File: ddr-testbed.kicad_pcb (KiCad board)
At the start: 4 copper layers, 69.6 x 30 mm, 2 parts, among them J1 ddr4-sodimm-edge-connector, U1 MT53E256M16D1

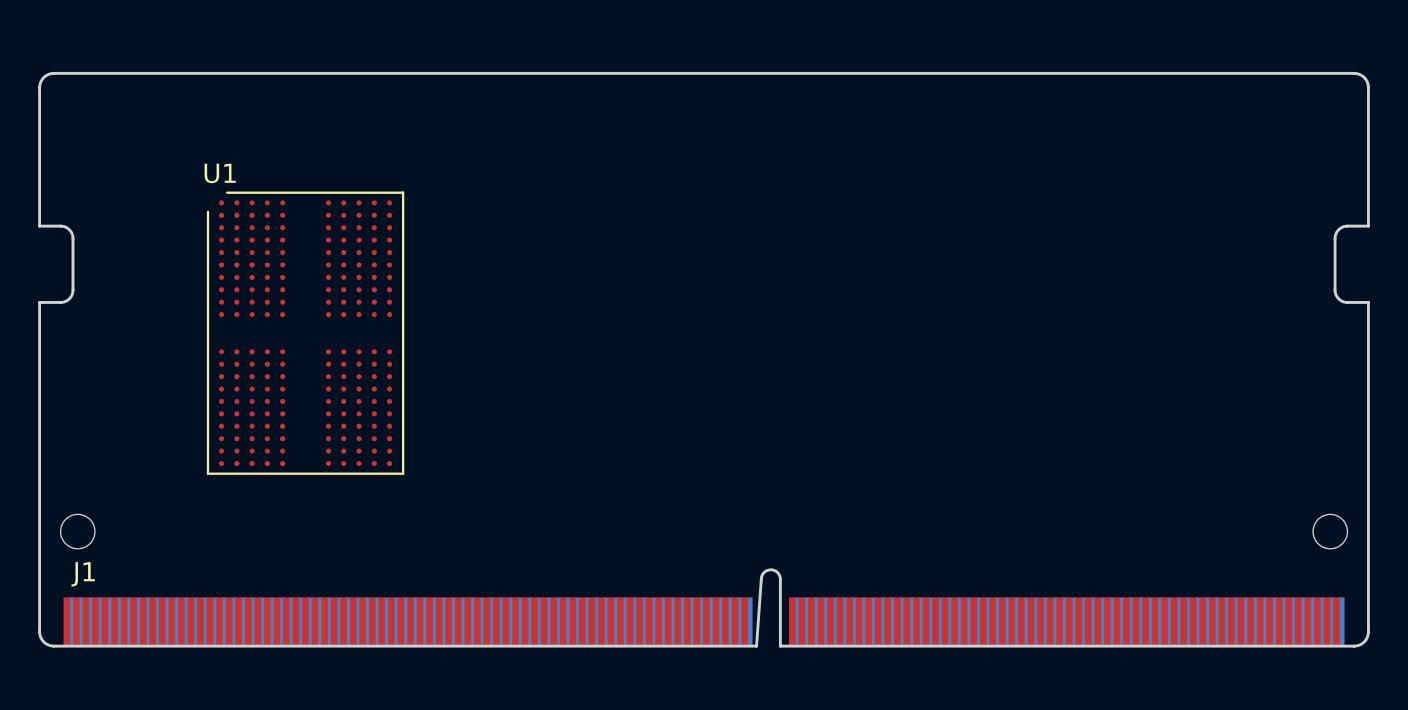
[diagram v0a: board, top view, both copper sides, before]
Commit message: Add initial component placement
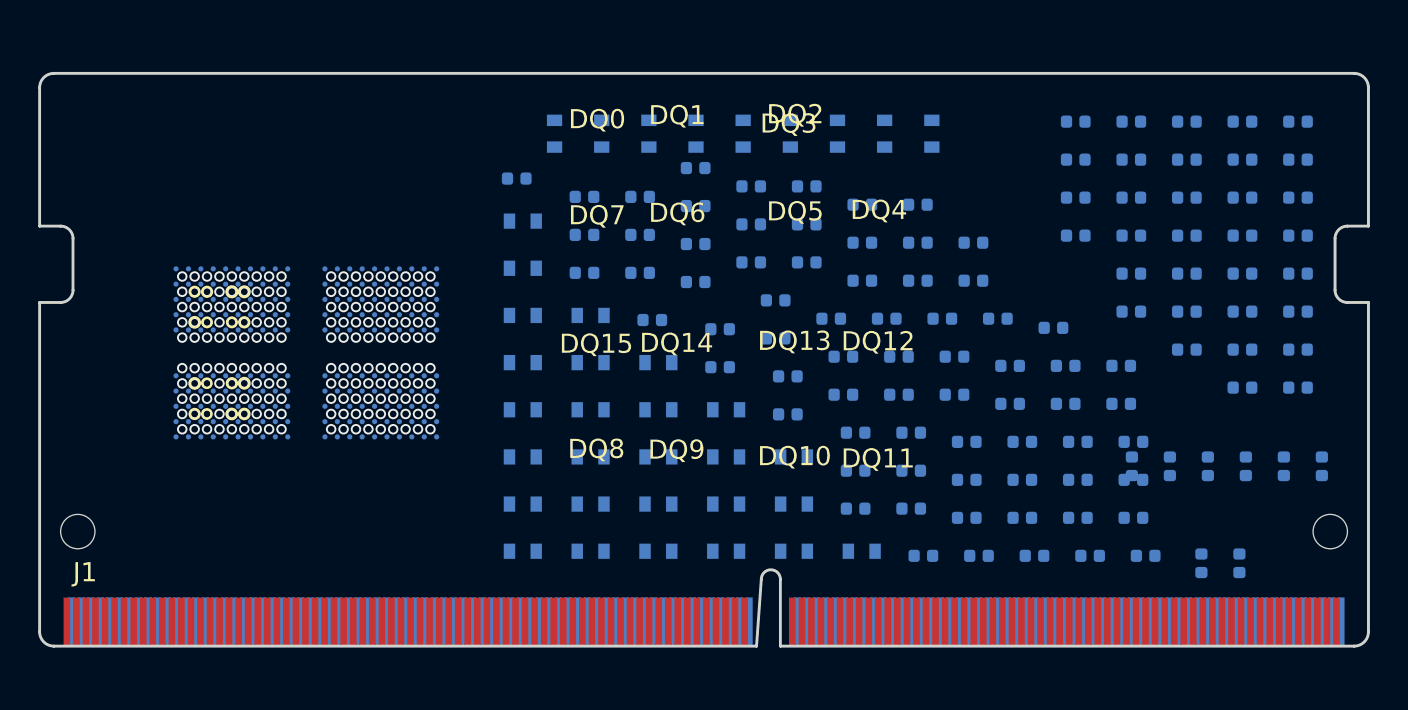
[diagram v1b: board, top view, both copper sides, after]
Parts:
- added C1: C_100p_0402, antmicro-footprints:0402-cap, B.Cu at (160.1, 76.5)
- added C10: C_10u_0603, antmicro-footprints:0603-cap, B.Cu at (136.8, 73.2)
- added C100: C_1u_0402, antmicro-footprints:0402-cap, B.Cu at (134.4, 75.0)
- added C101: C_1u_0402, antmicro-footprints:0402-cap, B.Cu at (141.5, 82.8)
- added C102: C_10u_0603, antmicro-footprints:0603-cap, B.Cu at (127.0, 73.2)
- added C103: C_10u_0603, antmicro-footprints:0603-cap, B.Cu at (139.5, 90.1)
- added C104: C_1u_0402, antmicro-footprints:0402-cap, B.Cu at (148.6, 89.3)
- added C105: C_1u_0402, antmicro-footprints:0402-cap, B.Cu at (151.5, 91.3)
- added C106: C_1u_0402, antmicro-footprints:0402-cap, B.Cu at (145.0, 84.8)
- added C107: C_1u_0402, antmicro-footprints:0402-cap, B.Cu at (134.4, 77.0)
- added C108: C_1u_0402, antmicro-footprints:0402-cap, B.Cu at (154.4, 93.3)
- added C109: C_1u_0402, antmicro-footprints:0402-cap, B.Cu at (142.7, 90.8)
- added C11: C_1u_0402, antmicro-footprints:0402-cap, B.Cu at (148.9, 78.9)
- added C110: C_1u_0402, antmicro-footprints:0402-cap, B.Cu at (147.9, 84.8)
- added C111: C_1u_0402, antmicro-footprints:0402-cap, B.Cu at (154.4, 91.3)
- added C112: C_1u_0402, antmicro-footprints:0402-cap, B.Cu at (151.5, 89.3)
- added C12: C_1u_0402, antmicro-footprints:0402-cap, B.Cu at (153.1, 83.3)
- added C13: C_10u_0603, antmicro-footprints:0603-cap, B.Cu at (132.4, 92.6)
- added C14: C_10u_0603, antmicro-footprints:0603-cap, B.Cu at (134.4, 73.2)
- added C15: C_100n_0402_6V3, antmicro-footprints:0402-cap, B.Cu at (156.7, 87.3)
- added C16: C_100n_0402_6V3, antmicro-footprints:0402-cap, B.Cu at (146.0, 76.9)
- added C17: C_1u_0402, antmicro-footprints:0402-cap, B.Cu at (145.0, 86.8)
- added C18: C_1u_0402, antmicro-footprints:0402-cap, B.Cu at (157.3, 89.3)
- added C19: C_10u_0603, antmicro-footprints:0603-cap, B.Cu at (131.9, 73.2)
- added C2: C_3p3_0402, antmicro-footprints:0402-res, B.Cu at (160.1, 72.5)
- added C20: C_10u_0603, antmicro-footprints:0603-cap, B.Cu at (136.0, 92.6)
- added C21: C_100n_0402_6V3, antmicro-footprints:0402-cap, B.Cu at (153.7, 85.3)
- added C22: C_1u_0402, antmicro-footprints:0402-cap, B.Cu at (146.0, 78.9)
- added C23: C_10u_0603, antmicro-footprints:0603-cap, B.Cu at (128.9, 87.6)
- added C24: C_100n_0402_6V3, antmicro-footprints:0402-cap, B.Cu at (157.3, 93.3)
- added C25: C_1u_0402, antmicro-footprints:0402-cap, B.Cu at (153.7, 87.3)
- added C26: C_10u_0603, antmicro-footprints:0603-cap, B.Cu at (132.4, 95.0)
- added C27: C_100n_0402_6V3, antmicro-footprints:0402-cap, B.Cu at (143.1, 76.9)
- added C28: C_1u_0402, antmicro-footprints:0402-cap, B.Cu at (157.3, 91.3)
- added C29: C_10u_0603, antmicro-footprints:0603-cap, B.Cu at (128.9, 95.0)
- added C3: C_10n_0402, antmicro-footprints:0402-cap, B.Cu at (165.2, 90.6)
- added C30: C_1u_0402, antmicro-footprints:0402-cap, B.Cu at (148.9, 80.9)
- added C31: C_100n_0402_6V3, antmicro-footprints:0402-cap, B.Cu at (143.1, 80.9)
- added C32: C_10u_0603, antmicro-footprints:0603-cap, B.Cu at (125.3, 82.7)
- added C33: C_10u_0603, antmicro-footprints:0603-cap, B.Cu at (128.9, 82.7)
- added C34: C_1u_0402, antmicro-footprints:0402-cap, B.Cu at (144.4, 82.8)
- added C35: C_100n_0402_6V3, antmicro-footprints:0402-cap, B.Cu at (137.3, 79.9)
- added C36: C_1u_0402, antmicro-footprints:0402-cap, B.Cu at (157.9, 95.3)
- added C37: C_100n_0402_6V3, antmicro-footprints:0402-cap, B.Cu at (140.2, 77.9)
- added C38: C_10u_0603, antmicro-footprints:0603-cap, B.Cu at (132.4, 87.6)
- added C39: C_10u_0603, antmicro-footprints:0603-cap, B.Cu at (128.9, 85.2)
- added C4: C_100n_0402_6V3, antmicro-footprints:0402-cap, B.Cu at (161.2, 90.6)
- added C40: C_1u_0402, antmicro-footprints:0402-cap, B.Cu at (137.3, 75.9)
- added C41: C_1u_0402, antmicro-footprints:0402-cap, B.Cu at (148.6, 91.3)
- added C42: C_100n_0402_6V3, antmicro-footprints:0402-cap, B.Cu at (142.1, 84.8)
- added C43: C_100n_0402_6V3, antmicro-footprints:0402-cap, B.Cu at (138.6, 83.9)
- added C44: C_10u_0603, antmicro-footprints:0603-cap, B.Cu at (132.4, 90.1)
- added C45: C_10u_0603, antmicro-footprints:0603-cap, B.Cu at (136.0, 95.0)
- added C46: C_1u_0402, antmicro-footprints:0402-cap, B.Cu at (125.0, 75.5)
- added C47: C_1u_0402, antmicro-footprints:0402-cap, B.Cu at (128.5, 80.5)
- added C48: C_100n_0402_6V3, antmicro-footprints:0402-cap, B.Cu at (132.1, 82.9)
- added C49: C_10u_0603, antmicro-footprints:0603-cap, B.Cu at (125.3, 95.0)
- added C5: C_1u_0402, antmicro-footprints:0402-cap, B.Cu at (151.5, 93.3)
- added C50: C_100n_0402_6V3, antmicro-footprints:0402-cap, B.Cu at (146.3, 95.3)
- added C51: C_10u_0603, antmicro-footprints:0603-cap, B.Cu at (132.4, 85.2)
- added C52: C_1u_0402, antmicro-footprints:0402-cap, B.Cu at (142.7, 92.8)
- added C53: C_10u_0603, antmicro-footprints:0603-cap, B.Cu at (139.5, 92.6)
- added C54: C_1u_0402, antmicro-footprints:0402-cap, B.Cu at (154.4, 89.3)
- added C55: C_100n_0402_6V3, antmicro-footprints:0402-cap, B.Cu at (131.4, 80.5)
- added C56: C_100n_0402_6V3, antmicro-footprints:0402-cap, B.Cu at (128.5, 78.5)
- added C57: C_10u_0603, antmicro-footprints:0603-cap, B.Cu at (139.5, 95.0)
- added C58: C_1u_0402, antmicro-footprints:0402-cap, B.Cu at (150.2, 82.8)
- added C59: C_1u_0402, antmicro-footprints:0402-cap, B.Cu at (150.8, 87.3)
- added C6: C_10u_0603, antmicro-footprints:0603-cap, B.Cu at (125.3, 90.1)
- added C60: C_10u_0603, antmicro-footprints:0603-cap, B.Cu at (136.0, 90.1)
- added C61: C_100n_0402_6V3, antmicro-footprints:0402-cap, B.Cu at (147.3, 82.8)
- added C62: C_1u_0402, antmicro-footprints:0402-cap, B.Cu at (143.1, 78.9)
- added C63: C_1u_0402, antmicro-footprints:0402-cap, B.Cu at (140.2, 75.9)
- added C64: C_10u_0603, antmicro-footprints:0603-cap, B.Cu at (125.3, 77.7)
- added C65: C_1u_0402, antmicro-footprints:0402-cap, B.Cu at (150.8, 85.3)
- added C66: C_1u_0402, antmicro-footprints:0402-cap, B.Cu at (146.0, 80.9)
- added C67: C_10u_0603, antmicro-footprints:0603-cap, B.Cu at (125.3, 87.6)
- added C68: C_1u_0402, antmicro-footprints:0402-cap, B.Cu at (134.4, 80.9)
- added C69: C_10u_0603, antmicro-footprints:0603-cap, B.Cu at (125.3, 85.2)
- added C7: C_1u_0402, antmicro-footprints:0402-cap, B.Cu at (140.2, 79.9)
- added C70: C_1u_0402, antmicro-footprints:0402-cap, B.Cu at (139.2, 85.9)
- added C71: C_1u_0402, antmicro-footprints:0402-cap, B.Cu at (142.7, 88.8)
- added C72: C_10u_0603, antmicro-footprints:0603-cap, B.Cu at (143.1, 95.0)
- added C73: C_1u_0402, antmicro-footprints:0402-cap, B.Cu at (149.2, 95.3)
- added C74: C_10u_0603, antmicro-footprints:0603-cap, B.Cu at (125.3, 80.2)
- added C75: C_1u_0402, antmicro-footprints:0402-cap, B.Cu at (135.6, 83.4)
- added C76: C_1u_0402, antmicro-footprints:0402-cap, B.Cu at (131.4, 78.5)
- added C77: C_10u_0603, antmicro-footprints:0603-cap, B.Cu at (129.4, 73.2)
- added C78: C_1u_0402, antmicro-footprints:0402-cap, B.Cu at (152.1, 95.3)
- added C79: C_1u_0402, antmicro-footprints:0402-cap, B.Cu at (128.5, 76.5)
- added C8: C_10u_0603, antmicro-footprints:0603-cap, B.Cu at (128.9, 92.6)
- added C80: C_10u_0603, antmicro-footprints:0603-cap, B.Cu at (136.0, 87.6)
- added C81: C_1u_0402, antmicro-footprints:0402-cap, B.Cu at (145.7, 92.8)
- added C82: C_1u_0402, antmicro-footprints:0402-cap, B.Cu at (145.7, 90.8)
- added C83: C_10u_0603, antmicro-footprints:0603-cap, B.Cu at (144.3, 73.2)
- added C84: C_1u_0402, antmicro-footprints:0402-cap, B.Cu at (139.2, 87.9)
- added C85: C_1u_0402, antmicro-footprints:0402-cap, B.Cu at (131.4, 76.5)
- added C86: C_10u_0603, antmicro-footprints:0603-cap, B.Cu at (125.3, 92.6)
- added C87: C_1u_0402, antmicro-footprints:0402-cap, B.Cu at (148.6, 93.3)
- added C88: C_1u_0402, antmicro-footprints:0402-cap, B.Cu at (134.4, 78.9)
- added C89: C_10u_0603, antmicro-footprints:0603-cap, B.Cu at (139.3, 73.2)
- added C9: C_100n_0402_6V3, antmicro-footprints:0402-cap, B.Cu at (156.7, 85.3)
- added C90: C_1u_0402, antmicro-footprints:0402-cap, B.Cu at (142.1, 86.8)
- added C91: C_1u_0402, antmicro-footprints:0402-cap, B.Cu at (135.6, 85.4)
- added C92: C_10u_0603, antmicro-footprints:0603-cap, B.Cu at (146.7, 73.2)
- added C93: C_1u_0402, antmicro-footprints:0402-cap, B.Cu at (138.6, 81.9)
- added C94: C_1u_0402, antmicro-footprints:0402-cap, B.Cu at (145.7, 88.8)
- added C95: C_10u_0603, antmicro-footprints:0603-cap, B.Cu at (128.9, 90.1)
- added C96: C_1u_0402, antmicro-footprints:0402-cap, B.Cu at (147.9, 86.8)
- added C97: C_1u_0402, antmicro-footprints:0402-cap, B.Cu at (155.0, 95.3)
- added C98: C_10u_0603, antmicro-footprints:0603-cap, B.Cu at (141.8, 73.2)
- added C99: C_1u_0402, antmicro-footprints:0402-cap, B.Cu at (137.3, 77.9)
- added R1: R_240R_0402, antmicro-footprints:0402-res, B.Cu at (157.2, 82.5)
- added R10: R_75R_0402, antmicro-footprints:0402-res, B.Cu at (157.2, 74.5)
- added R11: R_0R_0402, antmicro-footprints:0402-res, B.Cu at (165.9, 86.5)
- added R12: R_0R_0402, antmicro-footprints:0402-res, B.Cu at (163.0, 82.5)
- added R13: R_40R2_0402, antmicro-footprints:0402-res, B.Cu at (154.3, 74.5)
- added R14: R_40R2_0402, antmicro-footprints:0402-res, B.Cu at (165.9, 84.5)
- added R15: R_40R2_0402, antmicro-footprints:0402-res, B.Cu at (157.2, 76.5)
- added R16: R_40R2_0402, antmicro-footprints:0402-res, B.Cu at (160.1, 78.5)
- added R17: R_40R2_0402, antmicro-footprints:0402-res, B.Cu at (163.0, 80.5)
- added R18: R_40R2_0402, antmicro-footprints:0402-res, B.Cu at (167.2, 90.6)
- added R19: R_40R2_0402, antmicro-footprints:0402-res, B.Cu at (154.3, 72.5)
- added R2: R_120R_0402, antmicro-footprints:0402-res, B.Cu at (160.1, 84.5)
- added R20: R_40R2_0402, antmicro-footprints:0402-res, B.Cu at (165.9, 82.5)
- added R21: R_40R2_0402, antmicro-footprints:0402-res, B.Cu at (163.0, 78.5)
- added R22: R_40R2_0402, antmicro-footprints:0402-res, B.Cu at (165.9, 80.5)
- added R23: R_40R2_0402, antmicro-footprints:0402-res, B.Cu at (157.2, 72.5)
- added R24: R_40R2_0402, antmicro-footprints:0402-res, B.Cu at (163.2, 90.6)
- added R25: R_40R2_0402, antmicro-footprints:0402-res, B.Cu at (160.1, 74.5)
- added R26: R_40R2_0402, antmicro-footprints:0402-res, B.Cu at (163.0, 76.5)
- added R27: R_0R_0402, antmicro-footprints:0402-res, B.Cu at (165.9, 78.5)
- added R28: R_0R_0402, antmicro-footprints:0402-res, B.Cu at (160.8, 95.7)
- added R29: R_0R_0402, antmicro-footprints:0402-res, B.Cu at (160.1, 80.5)
- added R3: R_0R_0402, antmicro-footprints:0402-res, B.Cu at (154.3, 78.5)
- added R30: R_40R2_0402, antmicro-footprints:0402-res, B.Cu at (163.0, 74.5)
- added R31: R_0R_0402, antmicro-footprints:0402-res, B.Cu at (165.9, 76.5)
- added R32: R_40R2_0402, antmicro-footprints:0402-res, B.Cu at (159.2, 90.6)
- added R33: R_80R6_0402, antmicro-footprints:0402-res, B.Cu at (163.0, 72.5)
- added R34: R_80R6_0402, antmicro-footprints:0402-res, B.Cu at (165.9, 74.5)
- added R35: R_4k7_0402, antmicro-footprints:0402-res, B.Cu at (157.2, 90.6)
- added R36: R_0R_0402, antmicro-footprints:0402-res, B.Cu at (162.8, 95.7)
- added R37: R_40R2_0402, antmicro-footprints:0402-res, B.Cu at (165.9, 72.5)
- added R4: R_0R_0402, antmicro-footprints:0402-res, B.Cu at (157.2, 80.5)
- added R5: R_0R_0402, antmicro-footprints:0402-res, B.Cu at (163.0, 86.5)
- added R6: R_40R2_0402, antmicro-footprints:0402-res, B.Cu at (160.1, 82.5)
- added R7: R_40R2_0402, antmicro-footprints:0402-res, B.Cu at (163.0, 84.5)
- added R8: R_40R2_0402, antmicro-footprints:0402-res, B.Cu at (154.3, 76.5)
- added R9: R_40R2_0402, antmicro-footprints:0402-res, B.Cu at (157.2, 78.5)
- U1: moved to B.Cu
- moved U1 1.03 mm to (114.0, 84.6), turned to 270 degrees
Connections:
- net /DQ2 renamed /DQ02
- net Net-(J1-Pad113) renamed /BG0
- net Net-(J1-Pad114) renamed /ACT_N
- net Net-(J1-Pad115) renamed /BG1
- net Net-(J1-Pad134) renamed /EVENT_N
- net Net-(J1-Pad143) renamed /PARITY
- net Net-(J1-Pad145) renamed /BA1
- net Net-(J1-Pad149) renamed /CS0_N
- net Net-(J1-Pad150) renamed /BA0
- net Net-(J1-Pad253) renamed /SCL
- net Net-(J1-Pad254) renamed /SDA
- net Net-(J1-Pad255) renamed VDDSPD
- net Net-(J1-Pad256) renamed /SA0
- J1 pad 1: Net-(J1-Pad1) -> GND
- J1 pad 10: Net-(J1-Pad10) -> GND
- J1 pad 102: Net-(J1-Pad102) -> GND
- J1 pad 103: Net-(J1-Pad103) -> GND
- J1 pad 106: Net-(J1-Pad106) -> GND
- J1 pad 107: Net-(J1-Pad107) -> GND
- J1 pad 108: Net-(J1-Pad108) -> /RESET_CONN_N
- J1 pad 109: Net-(J1-Pad109) -> /CKE_0
- J1 pad 11: Net-(J1-Pad11) -> /DQS0_C
- J1 pad 110: Net-(J1-Pad110) -> /CKE_1
- J1 pad 111: Net-(J1-Pad111) -> DDRVCC
- J1 pad 112: Net-(J1-Pad112) -> DDRVCC
- J1 pad 116: Net-(J1-Pad116) -> /ALERT_N
- J1 pad 117: Net-(J1-Pad117) -> DDRVCC
- J1 pad 118: Net-(J1-Pad118) -> DDRVCC
- J1 pad 119: Net-(J1-Pad119) -> /CA2_B
- J1 pad 12: Net-(J1-Pad12) -> /DM0_N
- J1 pad 120: Net-(J1-Pad120) -> /CA1_B
- J1 pad 123: Net-(J1-Pad123) -> DDRVCC
- J1 pad 124: Net-(J1-Pad124) -> DDRVCC
- J1 pad 126: Net-(J1-Pad126) -> /CA5_A
- J1 pad 128: Net-(J1-Pad128) -> /CA4_A
- J1 pad 129: Net-(J1-Pad129) -> DDRVCC
- J1 pad 13: Net-(J1-Pad13) -> /DQS0_T
- J1 pad 130: Net-(J1-Pad130) -> DDRVCC
- J1 pad 131: Net-(J1-Pad131) -> /CA3_A
- J1 pad 132: Net-(J1-Pad132) -> /CA2_A
- J1 pad 133: Net-(J1-Pad133) -> /CA1_A
- J1 pad 135: Net-(J1-Pad135) -> DDRVCC
- J1 pad 136: Net-(J1-Pad136) -> DDRVCC
- J1 pad 137: Net-(J1-Pad137) -> /CK0_T
- J1 pad 138: Net-(J1-Pad138) -> /CK1_T
- J1 pad 139: Net-(J1-Pad139) -> /CK0_C
- J1 pad 14: Net-(J1-Pad14) -> GND
- J1 pad 140: Net-(J1-Pad140) -> /CK1_C
- J1 pad 141: Net-(J1-Pad141) -> DDRVCC
- J1 pad 142: Net-(J1-Pad142) -> DDRVCC
- J1 pad 144: Net-(J1-Pad144) -> /CA0_A
- J1 pad 146: Net-(J1-Pad146) -> /CA0_B
- J1 pad 147: Net-(J1-Pad147) -> DDRVCC
- J1 pad 148: Net-(J1-Pad148) -> DDRVCC
- J1 pad 15: Net-(J1-Pad15) -> GND
- J1 pad 151: Net-(J1-Pad151) -> /CA4_B
- J1 pad 153: Net-(J1-Pad153) -> DDRVCC
- J1 pad 154: Net-(J1-Pad154) -> DDRVCC
- J1 pad 155: Net-(J1-Pad155) -> /ODT0
- J1 pad 156: Net-(J1-Pad156) -> /CA5_B
- J1 pad 157: Net-(J1-Pad157) -> /CS_1_N
- J1 pad 158: Net-(J1-Pad158) -> /CA3_B
- J1 pad 159: Net-(J1-Pad159) -> DDRVCC
- J1 pad 16: /DQ4 -> /DQ06
- J1 pad 160: Net-(J1-Pad160) -> DDRVCC
- J1 pad 161: Net-(J1-Pad161) -> /ODT1
- J1 pad 163: Net-(J1-Pad163) -> DDRVCC
- J1 pad 164: Net-(J1-Pad164) -> /VREFCA
- J1 pad 166: Net-(J1-Pad166) -> /SA1
- J1 pad 167: Net-(J1-Pad167) -> GND
- J1 pad 168: Net-(J1-Pad168) -> GND
- J1 pad 17: /DQ6 -> /DQ07
- J1 pad 171: Net-(J1-Pad171) -> GND
- J1 pad 172: Net-(J1-Pad172) -> GND
- J1 pad 175: Net-(J1-Pad175) -> GND
- J1 pad 176: Net-(J1-Pad176) -> GND
- J1 pad 18: Net-(J1-Pad18) -> GND
- J1 pad 180: Net-(J1-Pad180) -> GND
- J1 pad 181: Net-(J1-Pad181) -> GND
- J1 pad 184: Net-(J1-Pad184) -> GND
- J1 pad 185: Net-(J1-Pad185) -> GND
- J1 pad 188: Net-(J1-Pad188) -> GND
- J1 pad 189: Net-(J1-Pad189) -> GND
- J1 pad 19: Net-(J1-Pad19) -> GND
- J1 pad 192: Net-(J1-Pad192) -> GND
- J1 pad 193: Net-(J1-Pad193) -> GND
- J1 pad 196: Net-(J1-Pad196) -> GND
- J1 pad 197: Net-(J1-Pad197) -> GND
- J1 pad 2: Net-(J1-Pad2) -> GND
- J1 pad 201: Net-(J1-Pad201) -> GND
- J1 pad 202: Net-(J1-Pad202) -> GND
- J1 pad 205: Net-(J1-Pad205) -> GND
- J1 pad 206: Net-(J1-Pad206) -> GND
- J1 pad 209: Net-(J1-Pad209) -> GND
- J1 pad 21: /DQ0 -> /DQ03
- J1 pad 210: Net-(J1-Pad210) -> GND
- J1 pad 213: Net-(J1-Pad213) -> GND
- J1 pad 214: Net-(J1-Pad214) -> GND
- J1 pad 217: Net-(J1-Pad217) -> GND
- J1 pad 218: Net-(J1-Pad218) -> GND
- J1 pad 22: Net-(J1-Pad22) -> GND
- J1 pad 222: Net-(J1-Pad222) -> GND
- J1 pad 223: Net-(J1-Pad223) -> GND
- J1 pad 226: Net-(J1-Pad226) -> GND
- J1 pad 227: Net-(J1-Pad227) -> GND
- J1 pad 23: Net-(J1-Pad23) -> GND
- J1 pad 230: Net-(J1-Pad230) -> GND
- J1 pad 231: Net-(J1-Pad231) -> GND
- J1 pad 234: Net-(J1-Pad234) -> GND
- J1 pad 235: Net-(J1-Pad235) -> GND
- J1 pad 238: Net-(J1-Pad238) -> GND
- J1 pad 239: Net-(J1-Pad239) -> GND
- J1 pad 24: Net-(J1-Pad24) -> /DQ12
- J1 pad 243: Net-(J1-Pad243) -> GND
- J1 pad 244: Net-(J1-Pad244) -> GND
- J1 pad 247: Net-(J1-Pad247) -> GND
- J1 pad 248: Net-(J1-Pad248) -> GND
- J1 pad 25: Net-(J1-Pad25) -> /DQ13
- J1 pad 251: Net-(J1-Pad251) -> GND
- J1 pad 252: Net-(J1-Pad252) -> GND
- J1 pad 257: Net-(J1-Pad257) -> VPP
- J1 pad 258: Net-(J1-Pad258) -> VTT
- J1 pad 259: Net-(J1-Pad259) -> VPP
- J1 pad 26: Net-(J1-Pad26) -> GND
- J1 pad 260: Net-(J1-Pad260) -> /SA1
- J1 pad 27: Net-(J1-Pad27) -> GND
- J1 pad 28: Net-(J1-Pad28) -> /DQ08
- J1 pad 29: Net-(J1-Pad29) -> /DQ09
- J1 pad 3: /DQ7 -> /DQ05
- J1 pad 30: Net-(J1-Pad30) -> GND
- J1 pad 31: Net-(J1-Pad31) -> GND
- J1 pad 32: Net-(J1-Pad32) -> /DQS1_C
- J1 pad 33: Net-(J1-Pad33) -> /DM1_N
- J1 pad 34: Net-(J1-Pad34) -> /DQS1_T
- J1 pad 35: Net-(J1-Pad35) -> GND
- J1 pad 36: Net-(J1-Pad36) -> GND
- J1 pad 37: Net-(J1-Pad37) -> /DQ15
- J1 pad 38: Net-(J1-Pad38) -> /DQ14
- J1 pad 39: Net-(J1-Pad39) -> GND
- J1 pad 4: /DQ5 -> /DQ04
- J1 pad 40: Net-(J1-Pad40) -> GND
- J1 pad 41: Net-(J1-Pad41) -> /DQ10
- J1 pad 42: Net-(J1-Pad42) -> /DQ11
- J1 pad 43: Net-(J1-Pad43) -> GND
- J1 pad 44: Net-(J1-Pad44) -> GND
- J1 pad 45: Net-(J1-Pad45) -> /DQ21
- J1 pad 46: Net-(J1-Pad46) -> /DQ20
- J1 pad 47: Net-(J1-Pad47) -> GND
- J1 pad 48: Net-(J1-Pad48) -> GND
- J1 pad 49: Net-(J1-Pad49) -> /DQ17
- J1 pad 5: Net-(J1-Pad5) -> GND
- J1 pad 50: Net-(J1-Pad50) -> /DQ16
- J1 pad 51: Net-(J1-Pad51) -> GND
- J1 pad 52: Net-(J1-Pad52) -> GND
- J1 pad 53: Net-(J1-Pad53) -> /DQS2_C
- J1 pad 54: Net-(J1-Pad54) -> /DM2_N
- J1 pad 55: Net-(J1-Pad55) -> /DQS2_T
- J1 pad 56: Net-(J1-Pad56) -> GND
- J1 pad 57: Net-(J1-Pad57) -> GND
- J1 pad 58: Net-(J1-Pad58) -> /DQ22
- J1 pad 59: Net-(J1-Pad59) -> /DQ23
- J1 pad 6: Net-(J1-Pad6) -> GND
- J1 pad 60: Net-(J1-Pad60) -> GND
- J1 pad 61: Net-(J1-Pad61) -> GND
- J1 pad 62: Net-(J1-Pad62) -> /DQ18
- J1 pad 63: Net-(J1-Pad63) -> /DQ19
- J1 pad 64: Net-(J1-Pad64) -> GND
- J1 pad 65: Net-(J1-Pad65) -> GND
- J1 pad 66: Net-(J1-Pad66) -> /DQ28
- J1 pad 67: Net-(J1-Pad67) -> /DQ29
- J1 pad 68: Net-(J1-Pad68) -> GND
- J1 pad 69: Net-(J1-Pad69) -> GND
- J1 pad 7: /DQ3 -> /DQ01
- J1 pad 70: Net-(J1-Pad70) -> /DQ24
- J1 pad 71: Net-(J1-Pad71) -> /DQ25
- J1 pad 72: Net-(J1-Pad72) -> GND
- J1 pad 73: Net-(J1-Pad73) -> GND
- J1 pad 74: Net-(J1-Pad74) -> /DQS3_C
- J1 pad 75: Net-(J1-Pad75) -> /DM3_N
- J1 pad 76: Net-(J1-Pad76) -> /DQS3_T
- J1 pad 77: Net-(J1-Pad77) -> GND
- J1 pad 78: Net-(J1-Pad78) -> GND
- J1 pad 79: Net-(J1-Pad79) -> /DQ30
- J1 pad 8: /DQ1 -> /DQ00
- J1 pad 80: Net-(J1-Pad80) -> /DQ31
- J1 pad 81: Net-(J1-Pad81) -> GND
- J1 pad 82: Net-(J1-Pad82) -> GND
- J1 pad 83: Net-(J1-Pad83) -> /DQ26
- J1 pad 84: Net-(J1-Pad84) -> /DQ27
- J1 pad 85: Net-(J1-Pad85) -> GND
- J1 pad 86: Net-(J1-Pad86) -> GND
- J1 pad 89: Net-(J1-Pad89) -> GND
- J1 pad 9: Net-(J1-Pad9) -> GND
- J1 pad 90: Net-(J1-Pad90) -> GND
- J1 pad 93: Net-(J1-Pad93) -> GND
- J1 pad 94: Net-(J1-Pad94) -> GND
- J1 pad 98: Net-(J1-Pad98) -> GND
- J1 pad 99: Net-(J1-Pad99) -> GND
- U1 pad AA11: Net-(U1-PadAA11) -> /DQ24
- U1 pad AA2: Net-(U1-PadAA2) -> /DQ16
- U1 pad AA4: Net-(U1-PadAA4) -> /DQ23
- U1 pad AA9: Net-(U1-PadAA9) -> /DQ31
- U1 pad B11: /DQ8 -> /DQ08
- U1 pad B2: /DQ0 -> /DQ00
- U1 pad B4: /DQ7 -> /DQ07
- U1 pad C10: Net-(U1-PadC10) -> /DM1_N
- U1 pad C11: /DQ9 -> /DQ09
- U1 pad C2: /DQ1 -> /DQ01
- U1 pad C3: Net-(U1-PadC3) -> /DM0_N
- U1 pad C4: /DQ6 -> /DQ06
- U1 pad D10: Net-(U1-PadD10) -> /DQS1_T
- U1 pad D3: Net-(U1-PadD3) -> /DQS0_T
- U1 pad E10: Net-(U1-PadE10) -> /DQS1_C
- U1 pad E3: Net-(U1-PadE3) -> /DQS0_C
- U1 pad E4: /DQ5 -> /DQ05
- U1 pad F2: /DQ3 -> /DQ03
- U1 pad F4: /DQ4 -> /DQ04
- U1 pad G2: Net-(U1-PadG2) -> /ODT0_A
- U1 pad H10: Net-(U1-PadH10) -> /CA3_A
- U1 pad H11: Net-(U1-PadH11) -> /CA4_A
- U1 pad H2: Net-(U1-PadH2) -> /CA0_A
- U1 pad H4: Net-(U1-PadH4) -> /CS0_N_A
- U1 pad H9: Net-(U1-PadH9) -> /CA2_A
- U1 pad J11: Net-(U1-PadJ11) -> /CA5_A
- U1 pad J2: Net-(U1-PadJ2) -> /CA1_A
- U1 pad J4: Net-(U1-PadJ4) -> /CKE0_A
- U1 pad J8: Net-(U1-PadJ8) -> /CK0_T
- U1 pad J9: Net-(U1-PadJ9) -> /CK0_C
- U1 pad P11: Net-(U1-PadP11) -> /CA5_B
- U1 pad P2: Net-(U1-PadP2) -> /CA1_B
- U1 pad P4: Net-(U1-PadP4) -> /CKE0_B
- U1 pad P8: Net-(U1-PadP8) -> /CK1_T
- U1 pad P9: Net-(U1-PadP9) -> /CK1_C
- U1 pad R10: Net-(U1-PadR10) -> /CA3_B
- U1 pad R11: Net-(U1-PadR11) -> /CA4_B
- U1 pad R2: Net-(U1-PadR2) -> /CA0_B
- U1 pad R4: Net-(U1-PadR4) -> /CS0_N_B
- U1 pad R9: Net-(U1-PadR9) -> /CA2_B
- U1 pad T11: Net-(U1-PadT11) -> /MEMRST_N
- U1 pad T2: Net-(U1-PadT2) -> /ODT0_A
- U1 pad U11: Net-(U1-PadU11) -> /DQ27
- U1 pad U2: Net-(U1-PadU2) -> /DQ19
- U1 pad U4: Net-(U1-PadU4) -> /DQ20
- U1 pad U9: Net-(U1-PadU9) -> /DQ28
- U1 pad V10: Net-(U1-PadV10) -> /DQS3_C
- U1 pad V11: Net-(U1-PadV11) -> /DQ26
- U1 pad V2: Net-(U1-PadV2) -> /DQ18
- U1 pad V3: Net-(U1-PadV3) -> /DQS2_C
- U1 pad V4: Net-(U1-PadV4) -> /DQ21
- U1 pad V9: Net-(U1-PadV9) -> /DQ29
- U1 pad W10: Net-(U1-PadW10) -> /DQS3_T
- U1 pad W3: Net-(U1-PadW3) -> /DQS2_T
- U1 pad Y10: Net-(U1-PadY10) -> /DM3_N
- U1 pad Y11: Net-(U1-PadY11) -> /DQ25
- U1 pad Y2: Net-(U1-PadY2) -> /DQ17
- U1 pad Y3: Net-(U1-PadY3) -> /DM2_N
- U1 pad Y4: Net-(U1-PadY4) -> /DQ22
- U1 pad Y9: Net-(U1-PadY9) -> /DQ30
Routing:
- net Net-(U1-PadA12): vias 0 -> 45
- net (no net): vias 0 -> 135
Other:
- rule trace_min: 0.2 -> 0.15
- board text added: "DQ0"
- board text added: "DQ1"
- board text added: "DQ10"
- board text added: "DQ11"
- board text added: "DQ12"
- board text added: "DQ13"
- board text added: "DQ14"
- board text added: "DQ15"
- board text added: "DQ2"
- board text added: "DQ3"
- board text added: "DQ4"
- board text added: "DQ5"
- board text added: "DQ6"
- board text added: "DQ7"
- board text added: "DQ8"
- board text added: "DQ9"

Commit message: Add LPDDR4 Fanout and pinout tabele
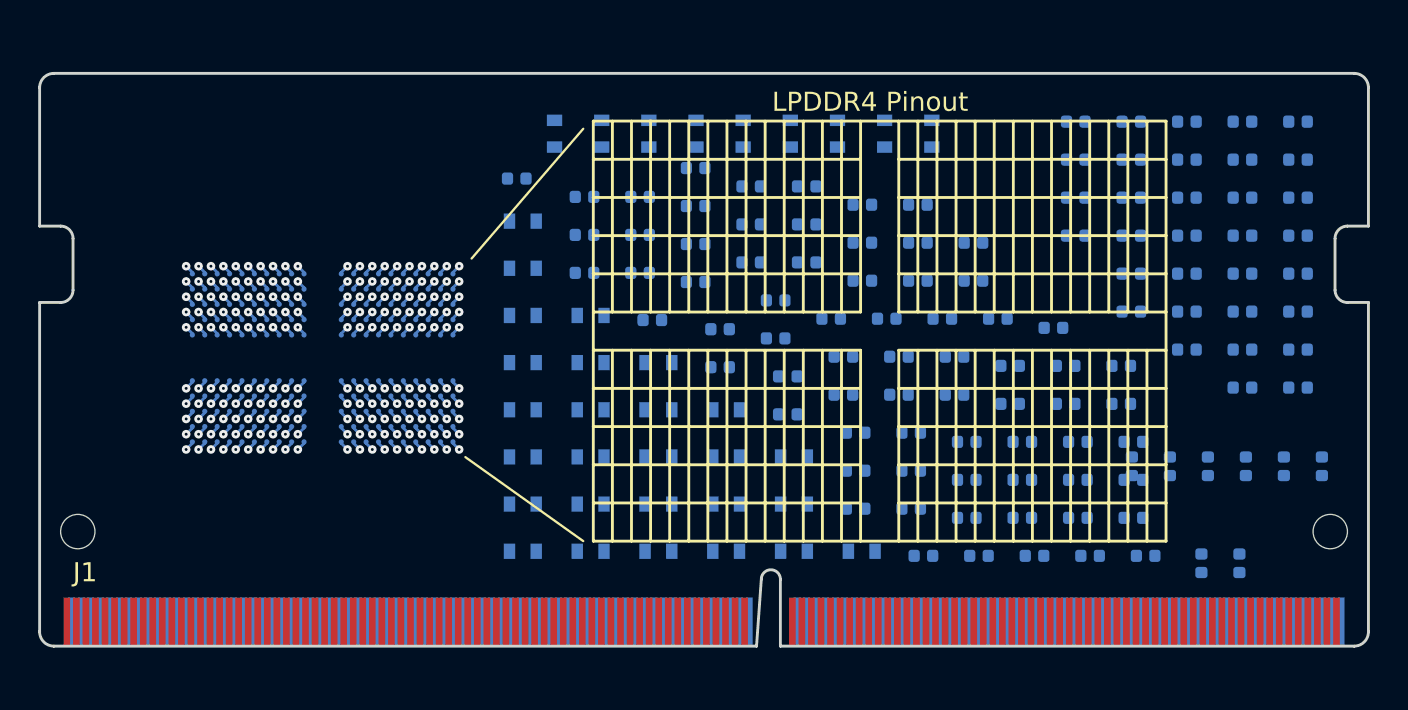
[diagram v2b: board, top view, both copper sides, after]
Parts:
- moved U1 0.89 mm to (114.8, 84.9)
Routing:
- net GND: track 0.00 -> 31.0 mm, vias 0 -> 58
- net DDRVCC: track 0.00 -> 27.8 mm, vias 0 -> 52
- net /ODT0_A: track 0.00 -> 1.07 mm, vias 0 -> 2
- net Net-(U1-PadP5): track 0.00 -> 0.53 mm, vias 0 -> 1
- net Net-(U1-PadN8): track 0.00 -> 0.53 mm, vias 0 -> 1
- net Net-(U1-PadN5): track 0.00 -> 0.53 mm, vias 0 -> 1
- net Net-(U1-PadJ5): track 0.00 -> 0.53 mm, vias 0 -> 1
- net Net-(U1-PadG11): track 0.00 -> 0.53 mm, vias 0 -> 1
- net Net-(U1-PadB12): track 0.00 -> 0.53 mm, vias 0 -> 1
- net Net-(U1-PadB1): track 0.00 -> 0.53 mm, vias 0 -> 1
- net Net-(U1-PadAA12): track 0.00 -> 0.53 mm, vias 0 -> 1
- net Net-(U1-PadAA1): track 0.00 -> 0.53 mm, vias 0 -> 1
- net Net-(U1-PadA8): track 0.00 -> 0.53 mm, vias 0 -> 1
- net Net-(U1-PadA12): track 0.00 -> 0.53 mm, vias 45 -> 1
- net Net-(U1-PadA11): track 0.00 -> 0.53 mm, vias 0 -> 1
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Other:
- net class Default: clearance 0.2 -> 0.15; trace_width 0.25 -> 0.15; via_dia 0.6 -> 0.45; via_drill 0.4 -> 0.15
- rule trace_clearance: 0.2 -> 0.15
- rule via_min_drill: 0.3 -> 0.15
- board text added: "LPDDR4 Pinout"
- board text removed: "DQ0"
- board text removed: "DQ1"
- board text removed: "DQ10"
- board text removed: "DQ11"
- board text removed: "DQ12"
- board text removed: "DQ13"
- board text removed: "DQ14"
- board text removed: "DQ15"
- board text removed: "DQ2"
- board text removed: "DQ3"
- board text removed: "DQ4"
- board text removed: "DQ5"
- board text removed: "DQ6"
- board text removed: "DQ7"
- board text removed: "DQ8"
- board text removed: "DQ9"

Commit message: Replace capacitors and place them on PCB
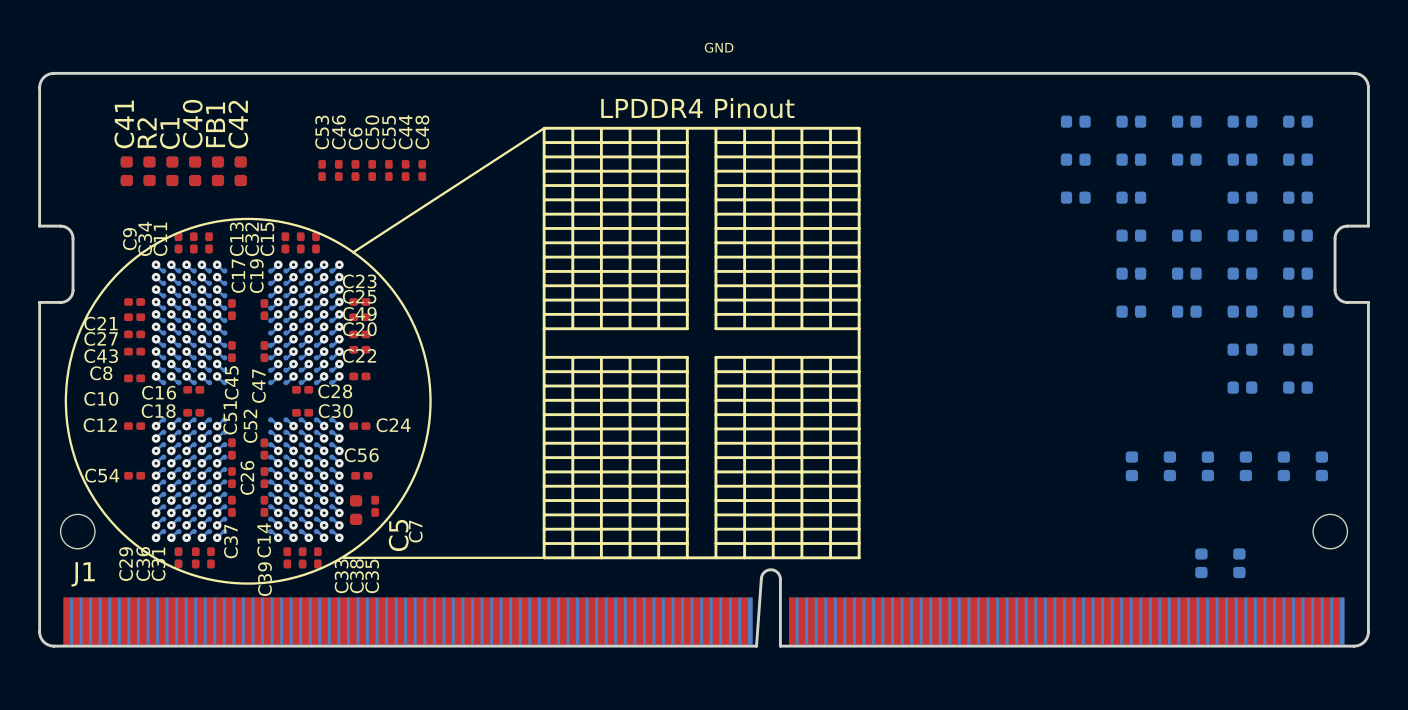
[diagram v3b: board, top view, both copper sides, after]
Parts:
- removed C100, C101, C104, C105, C106, C107, C108, C109, C110, C111, C112, C58, C59, C62, C63, C65, C66, C68, C70, C71, C73, C75, C76, C78, C79, C81, C82, C84, C85, C87, C88, C90, C91, C93, C94, C96, C97, C99: C_1u_0402, antmicro-footprints:0402-cap
- removed C102, C103, C57, C60, C64, C67, C69, C72, C74, C77, C80, C83, C86, C89, C92, C95, C98: C_10u_0603, antmicro-footprints:0603-cap
- removed C61: C_100n_0402_6V3, antmicro-footprints:0402-cap
- removed R3: R_0R_0402, antmicro-footprints:0402-res
- added FB1: BLM15PD121SN1D, antmicro-footprints:0402-res, F.Cu at (109.3, 75.1)
- C1: value C_100p_0402 -> C_10u_0402; moved to F.Cu
- C10, C13, C14, C19, C20, C23, C26, C29, C32, C33, C38, C39, C45, C49, C51, C53, C8: value C_10u_0603 -> C_100n_0201; footprint antmicro-footprints:0603-cap -> antmicro-footprints:0201-res; moved to F.Cu
- C11, C12, C17, C18, C22, C25, C28, C30, C34, C36, C47, C52, C54: value C_1u_0402 -> C_100n_0201; footprint antmicro-footprints:0402-cap -> antmicro-footprints:0201-res; moved to F.Cu
- C15, C16, C21, C24, C27, C31, C35, C37, C43, C55, C56, C9: value C_100n_0402_6V3 -> C_100n_0201; footprint antmicro-footprints:0402-cap -> antmicro-footprints:0201-res; moved to F.Cu
- C40, C41, C5: value C_1u_0402 -> C_10u_0402; moved to F.Cu
- C42: value C_100n_0402_6V3 -> C_10u_0402; moved to F.Cu
- C44, C6: value C_10u_0603 -> C_1u_0201; footprint antmicro-footprints:0603-cap -> antmicro-footprints:0201-res; moved to F.Cu
- C46, C7: value C_1u_0402 -> C_1u_0201; footprint antmicro-footprints:0402-cap -> antmicro-footprints:0201-res; moved to F.Cu
- C48, C50: value C_100n_0402_6V3 -> C_1u_0201; footprint antmicro-footprints:0402-cap -> antmicro-footprints:0201-res; moved to F.Cu
- R2: value R_120R_0402 -> R_10k_0402; moved to F.Cu
- moved R2 55.1 mm to (105.8, 75.1), turned to 90 degrees
- moved C1 53.2 mm to (107.0, 75.1), turned to 90 degrees
- moved C9 49.8 mm to (107.3, 78.9), turned to 90 degrees
- moved C36 49.8 mm to (108.2, 95.4), turned to 270 degrees
- moved C54 49.4 mm to (105.0, 91.1), turned to 180 degrees
- moved C18 49.2 mm to (108.1, 87.8)
- moved C21 48.9 mm to (105.0, 82.0), turned to 180 degrees
- moved C12 48.4 mm to (105.0, 88.5), turned to 180 degrees
- moved C41 46.9 mm to (104.6, 75.1), turned to 90 degrees
- moved C28 43.8 mm to (113.8, 86.6), turned to 180 degrees
- moved C15 43.0 mm to (114.5, 78.9), turned to 90 degrees
- moved C24 40.8 mm to (116.8, 88.5)
- moved C11 40.0 mm to (108.9, 78.9), turned to 90 degrees
- moved C16 39.1 mm to (108.1, 86.6)
- moved C27 38.6 mm to (105.0, 82.8), turned to 180 degrees
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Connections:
- C1 pad 1: GND -> VDD2
- C1 pad 2: /MEMRST_N -> GND
- C10 pad 1: VPP -> VDD2
- C11 pad 1: VPP -> VDDQ
- C12 pad 1: VDD -> VDD2
- C13 pad 1: VDD -> VDDQ
- C14 pad 1: VPP -> VDD2
- C15 pad 1: VDD -> VDDQ
- C16 pad 1: VREFCA -> VDD2
- C16 pad 2: VDD -> GND
- C17 pad 1: VPP -> VDDQ
- C18 pad 1: VDD -> VDD2
- C19 pad 1: VDD -> VDDQ
- C20 pad 1: VPP -> VDD2
- C21 pad 1: VREFCA -> VDDQ
- C21 pad 2: VDD -> GND
- C22 pad 1: VPP -> VDD2
- C23 pad 1: VDD -> VDDQ
- C24 pad 1: VDD -> VDD2
- C25 pad 1: VDD -> VDDQ
- C26 pad 1: VPP -> VDD2
- C27 pad 1: VREFCA -> VDDQ
- C27 pad 2: VDD -> GND
- C28 pad 1: VPP -> VDD2
- C29 pad 1: VDD -> VDDQ
- C30 pad 1: VDD -> VDD2
- C31 pad 1: VDD -> VDDQ
- C32 pad 1: VPP -> VDD2
- C33 pad 1: VDD -> VDDQ
- C34 pad 1: VPP -> VDD2
- C35 pad 1: VREFCA -> VDDQ
- C35 pad 2: VDD -> GND
- C36 pad 1: VDD -> VDD2
- C37 pad 1: VDD -> VDDQ
- C38 pad 1: VPP -> VDD2
- C39 pad 1: VDD -> VDDQ
- C40 pad 1: VPP -> VDD2
- C41 pad 1: VDD -> VDD1
- C42 pad 1: VREFCA -> VDD2
- C42 pad 2: VDD -> GND
- C43 pad 1: VDD -> VDD1
- C44 pad 1: VPP -> VDD2
- C45 pad 1: VDD -> VDD1
- C46 pad 1: VPP -> VDD2
- C47 pad 1: VDD -> VDD1
- C48 pad 1: VREFCA -> VDD2
- C48 pad 2: VDD -> GND
- C49 pad 1: VPP -> VDD1
- C5 pad 1: VPP -> VDDQ
- C50 pad 1: VDD -> VDD2
- C51 pad 1: VDD -> VDD1
- C52 pad 1: VPP -> VDD1
- C53 pad 1: VPP -> VDD2
- C54 pad 1: VDD -> VDD1
- C55 pad 1: VREFCA -> VDD2
- C55 pad 2: VDD -> GND
- C56 pad 1: VDD -> VDD1
- C6 pad 1: VPP -> VDD2
- C7 pad 1: VDD -> VDDQ
- C8 pad 1: VDD -> VDD2
- C9 pad 1: VREFCA -> VDDQ
- C9 pad 2: VDD -> GND
- J1 pad 111: DDRVCC -> VDDQ
- J1 pad 112: DDRVCC -> VDDQ
- J1 pad 117: DDRVCC -> VDDQ
- J1 pad 118: DDRVCC -> VDDQ
- J1 pad 123: DDRVCC -> VDD1_A
- J1 pad 124: DDRVCC -> VDD1_A
- J1 pad 129: DDRVCC -> VDD1_A
- J1 pad 130: DDRVCC -> VDD1_A
- J1 pad 135: DDRVCC -> VDD2
- J1 pad 136: DDRVCC -> VDD2
- J1 pad 141: DDRVCC -> VDD2
- J1 pad 142: DDRVCC -> VDD2
- J1 pad 147: DDRVCC -> VDD2
- J1 pad 148: DDRVCC -> VDD2
- J1 pad 153: DDRVCC -> VDD2
- J1 pad 154: DDRVCC -> VDD2
- J1 pad 159: DDRVCC -> VDD2
- J1 pad 160: DDRVCC -> VDD2
- J1 pad 163: DDRVCC -> VDD2
- R1 pad 2: GND -> VDDQ
- R13 pad 1: /CKE0_A -> /CA0_A
- R14 pad 1: /CA5_A -> /CA1_A
- R15 pad 1: /CA4_A -> /CA2_A
- R17 pad 1: /CA2_A -> /CA4_A
- R18 pad 1: /CA1_A -> /CA5_A
- R19 pad 1: /CA0_A -> /CKE0_A
- R2 pad 1: /RESET_CONN_N -> VDDQ
- R2 pad 2: /MEMRST_N -> /ODT0_A
- R20 pad 1: /CKE0_B -> /CA0_B
- R21 pad 1: /CA5_B -> /CA1_B
- R22 pad 1: /CA4_B -> /CA2_B
- R24 pad 1: /CA2_B -> /CA4_B
- R25 pad 1: /CA1_B -> /CA5_B
- R26 pad 1: /CA0_B -> /CKE0_B
- R29 pad 1: /ODT0_A -> /ODT0_B
- R33 pad 1: DDRVCC -> VDDQ
- R34 pad 1: DDRVCC -> VDDQ
- U1 pad A4: DDRVCC -> VDD2
- U1 pad A9: DDRVCC -> VDD2
- U1 pad AA10: DDRVCC -> VDDQ
- U1 pad AA3: DDRVCC -> VDDQ
- U1 pad AA5: DDRVCC -> VDDQ
- U1 pad AA8: DDRVCC -> VDDQ
- U1 pad AB4: DDRVCC -> VDD2
- U1 pad AB9: DDRVCC -> VDD2
- U1 pad B10: DDRVCC -> VDDQ
- U1 pad B3: DDRVCC -> VDDQ
- U1 pad B5: DDRVCC -> VDDQ
- U1 pad B8: DDRVCC -> VDDQ
- U1 pad D1: DDRVCC -> VDDQ
- U1 pad D12: DDRVCC -> VDDQ
- U1 pad D5: DDRVCC -> VDDQ
- U1 pad D8: DDRVCC -> VDDQ
- U1 pad F1: DDRVCC -> VDD1
- U1 pad F10: DDRVCC -> VDDQ
- U1 pad F12: DDRVCC -> VDD1
- U1 pad F3: DDRVCC -> VDDQ
- U1 pad F5: DDRVCC -> VDD2
- U1 pad F8: DDRVCC -> VDD2
- U1 pad G4: DDRVCC -> VDD1
- U1 pad G9: DDRVCC -> VDD1
- U1 pad H1: DDRVCC -> VDD2
- U1 pad H12: DDRVCC -> VDD2
- U1 pad H5: DDRVCC -> VDD2
- U1 pad H8: DDRVCC -> VDD2
- U1 pad K1: DDRVCC -> VDD2
- U1 pad K10: DDRVCC -> VDD2
- U1 pad K12: DDRVCC -> VDD2
- U1 pad K3: DDRVCC -> VDD2
- U1 pad N1: DDRVCC -> VDD2
- U1 pad N10: DDRVCC -> VDD2
- U1 pad N12: DDRVCC -> VDD2
- U1 pad N3: DDRVCC -> VDD2
- U1 pad R1: DDRVCC -> VDD2
- U1 pad R12: DDRVCC -> VDD2
- U1 pad R5: DDRVCC -> VDD2
- U1 pad R8: DDRVCC -> VDD2
- U1 pad T2: /ODT0_A -> /ODT0_B
- U1 pad T4: DDRVCC -> VDD1
- U1 pad T9: DDRVCC -> VDD1
- U1 pad U1: DDRVCC -> VDD1
- U1 pad U10: DDRVCC -> VDDQ
- U1 pad U12: DDRVCC -> VDD1
- U1 pad U3: DDRVCC -> VDDQ
- U1 pad U5: DDRVCC -> VDD2
- U1 pad U8: DDRVCC -> VDD2
- U1 pad W1: DDRVCC -> VDDQ
- U1 pad W12: DDRVCC -> VDDQ
- U1 pad W5: DDRVCC -> VDDQ
- U1 pad W8: DDRVCC -> VDDQ
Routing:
- net DDRVCC: track 27.8 -> 0.00 mm, vias 52 -> 0
- net VDD2: track 0.00 -> 12.8 mm, vias 0 -> 24
- net VDDQ: track 0.00 -> 10.7 mm, vias 0 -> 20
- net VDD1: track 0.00 -> 4.28 mm, vias 0 -> 8
- net /ODT0_B: track 0.00 -> 0.53 mm, vias 0 -> 1
- net /ODT0_A: track 1.07 -> 0.53 mm, vias 2 -> 1
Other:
- board text added: "GND"
